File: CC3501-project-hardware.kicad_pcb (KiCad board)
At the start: 4 copper layers, 0 parts

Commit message: Recover autosave.
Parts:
- added C1: 22pF, Capacitor_SMD:C_0402_1005Metric, F.Cu at (469.1, 13.7)
- added C10: 100nF, Capacitor_SMD:C_0402_1005Metric, F.Cu at (449.4, 0.25)
- added C11: 100nF, Capacitor_SMD:C_0402_1005Metric, F.Cu at (449.4, 2.22)
- added C12: 100nF, Capacitor_SMD:C_0402_1005Metric, F.Cu at (449.4, 4.19)
- added C13: 100nF, Capacitor_SMD:C_0402_1005Metric, F.Cu at (449.4, 6.16)
- added C14: 100nF, Capacitor_SMD:C_0402_1005Metric, F.Cu at (449.4, 8.13)
- added C15: 100nF, Capacitor_SMD:C_0402_1005Metric, F.Cu at (452.2, 0.25)
- added C16: 100nF, Capacitor_SMD:C_0402_1005Metric, F.Cu at (452.2, 2.22)
- added C17: 100nF, Capacitor_SMD:C_0402_1005Metric, F.Cu at (452.2, 4.19)
- added C18: 100nF, Capacitor_SMD:C_0402_1005Metric, F.Cu at (404.7, 48.9)
- added C19: 10uF, Capacitor_SMD:C_0402_1005Metric, F.Cu at (384.0, 65.0)
- added C2: 10uF, Capacitor_SMD:C_0603_1608Metric, F.Cu at (473.7, 14.2)
- added C20: 100nF, Capacitor_SMD:C_0402_1005Metric, F.Cu at (384.0, 66.9)
- added C21: 10uF, Capacitor_SMD:C_0402_1005Metric, F.Cu at (384.0, 68.9)
- added C22: 100nF, Capacitor_SMD:C_0402_1005Metric, F.Cu at (384.0, 70.9)
- added C23: 22p NP0, Capacitor_SMD:C_0402_1005Metric, F.Cu at (392.0, 83.0)
- added C24: 22p NP0, Capacitor_SMD:C_0402_1005Metric, F.Cu at (392.0, 85.0)
- added C25: 62p NP0 2%, Capacitor_SMD:C_0805_2012Metric, F.Cu at (400.1, 83.6)
- added C26: 62p NP0 2%, Capacitor_SMD:C_0805_2012Metric, F.Cu at (400.1, 86.6)
- added C27: 56p, Capacitor_SMD:C_0603_1608Metric, F.Cu at (384.6, 83.3)
- added C28: 56p, Capacitor_SMD:C_0603_1608Metric, F.Cu at (384.6, 85.8)
- added C29: 270p NP0 2%, Capacitor_SMD:C_0603_1608Metric, F.Cu at (384.6, 88.3)
- added C3: 100nF, Capacitor_SMD:C_0402_1005Metric, F.Cu at (470.9, 48.3)
- added C30: 270p NP0 2%, Capacitor_SMD:C_0603_1608Metric, F.Cu at (384.6, 90.8)
- added C31: 270p NP0 2%, Capacitor_SMD:C_0603_1608Metric, F.Cu at (384.6, 93.4)
- added C32: 270p NP0 2%, Capacitor_SMD:C_0603_1608Metric, F.Cu at (384.6, 95.9)
- added C33: 100n X7R 10%, Capacitor_SMD:C_0603_1608Metric, F.Cu at (388.6, 83.3)
- added C34: 1n NP0 10%, Capacitor_SMD:C_0603_1608Metric, F.Cu at (388.6, 85.8)
- added C35: 100nF, Capacitor_SMD:C_0402_1005Metric, F.Cu at (392.0, 87.0)
- added C36: 100nF, Capacitor_SMD:C_0402_1005Metric, F.Cu at (392.0, 89.0)
- added C37: 100nF, Capacitor_SMD:C_0402_1005Metric, F.Cu at (392.0, 90.9)
- added C38: 100nF, Capacitor_SMD:C_0402_1005Metric, F.Cu at (392.0, 92.9)
- added C39: 100nF, Capacitor_SMD:C_0402_1005Metric, F.Cu at (384.0, 72.9)
- added C4: 33pF, Capacitor_SMD:C_0402_1005Metric, F.Cu at (487.1, 17.3)
- added C40: 100nF, Capacitor_SMD:C_0402_1005Metric, F.Cu at (384.0, 74.8)
- added C41: 100nF, Capacitor_SMD:C_0402_1005Metric, F.Cu at (384.0, 76.8)
- added C5: 33pF, Capacitor_SMD:C_0402_1005Metric, F.Cu at (491.5, 17.5)
- added C6: 10uF, Capacitor_SMD:C_0402_1005Metric, F.Cu at (451.1, 17.3)
- added C7: 1uF, Capacitor_SMD:C_0402_1005Metric, F.Cu at (470.9, 24.4)
- added C8: 1uF, Capacitor_SMD:C_0402_1005Metric, F.Cu at (473.9, 24.9)
- added C9: 100nF, Capacitor_SMD:C_0402_1005Metric, F.Cu at (446.5, 8.13)
- added D1: PRTR5V0U2X, Package_TO_SOT_SMD:SOT-143, F.Cu at (389.6, 37.8)
- added DS1: ILI9341, SamacSys_Parts:ILI9341, F.Cu at (342.8, 20.6)
- added J1: USB_C_Receptacle_USB2.0_16P, Connector_USB:USB_C_Receptacle_G-Switch_GT-USB-7010ASV, F.Cu at (453.0, 31.0)
- added J2: Conn_01x03_Socket, Connector_PinSocket_2.54mm:PinSocket_1x03_P2.54mm_Vertical, F.Cu at (406.6, 84.4)
- added J3: Conn_01x03_Socket, Connector_PinSocket_2.54mm:PinSocket_1x03_P2.54mm_Vertical, F.Cu at (411.2, 84.4)
- added J4: Conn_01x03_Socket, Connector_PinHeader_2.54mm:PinHeader_1x03_P2.54mm_Vertical, F.Cu at (394.5, 28.4)
- added J5: Conn_01x04_Socket, Connector_PinHeader_2.54mm:PinHeader_1x04_P2.54mm_Vertical, F.Cu at (377.9, 58.0)
- added J6: Conn_01x08_Socket, Connector_PinHeader_2.54mm:PinHeader_1x08_P2.54mm_Vertical, F.Cu at (377.9, 18.3)
- added J7: Conn_01x04, Connector_PinHeader_2.54mm:PinHeader_1x04_P2.54mm_Vertical, F.Cu at (387.7, 66.3)
- added J8: Conn_01x06_Socket, Connector_PinHeader_2.54mm:PinHeader_1x06_P2.54mm_Vertical, F.Cu at (377.9, 40.7)
- added JP1: SolderJumper_3_Bridged12, Jumper:SolderJumper-3_P1.3mm_Bridged12_RoundedPad1.0x1.5mm_NumberLabels, F.Cu at (413.6, 93.5)
- added JP4: SolderJumper_2_Bridged, Jumper:SolderJumper-2_P1.3mm_Bridged2Bar_RoundedPad1.0x1.5mm, F.Cu at (400.0, 77.4)
- added L1: 1uH, SamacSys_Parts:IND-SMD_L4.5-W4.0, F.Cu at (462.5, 19.6)
- added L2: 1uH, Inductor_SMD:L_0603_1608Metric, F.Cu at (388.6, 88.3)
- added L3: 1uH, Inductor_SMD:L_0603_1608Metric, F.Cu at (388.6, 90.8)
- added L4: 3.3uH, Inductor_SMD:L_0805_2012Metric, F.Cu at (387.7, 77.6)
- added P2: Header 1.27mm 2x5 PTH, Connector_PinHeader_1.27mm:PinHeader_2x05_P1.27mm_Vertical, F.Cu at (399.9, 43.7)
- added P3: Header 3, Connector_PinHeader_2.54mm:PinHeader_1x03_P2.54mm_Vertical, F.Cu at (393.4, 54.6)
- added Q1: SS8550, Package_TO_SOT_SMD:SOT-23, F.Cu at (392.5, 77.8)
- added Q3: AO3401A, Package_TO_SOT_SMD:SOT-23, F.Cu at (378.1, 76.0)
- added Q4: AO3401A, Package_TO_SOT_SMD:SOT-23, F.Cu at (383.8, 35.3)
- added R1: 5K1, Resistor_SMD:R_0201_0603Metric, F.Cu at (463.0, 34.6)
- added R10: 4.7k, Resistor_SMD:R_0603_1608Metric, F.Cu at (427.5, 74.4)
- added R11: 100, Resistor_SMD:R_0402_1005Metric, F.Cu at (431.8, 74.7)
- added R12: 100k, Resistor_SMD:R_0201_0603Metric, F.Cu at (477.1, 69.3)
- added R13: 27R, Resistor_SMD:R_0201_0603Metric, F.Cu at (376.9, 79.1)
- added R14: 100, Resistor_SMD:R_0402_1005Metric, F.Cu at (396.4, 76.6)
- added R15: 100, Resistor_SMD:R_0402_1005Metric, F.Cu at (396.4, 78.6)
- added R16: 20k, Resistor_SMD:R_0805_2012Metric, F.Cu at (400.7, 65.5)
- added R17: 8.2k, Resistor_SMD:R_0805_2012Metric, F.Cu at (400.7, 68.4)
- added R18: 10k, Resistor_SMD:R_0805_2012Metric, F.Cu at (397.9, 56.7)
- added R19: 10k, Resistor_SMD:R_0805_2012Metric, F.Cu at (400.7, 71.4)
- added R2: 5K1, Resistor_SMD:R_0201_0603Metric, F.Cu at (463.0, 36.3)
- added R20: 10k, Resistor_SMD:R_0805_2012Metric, F.Cu at (377.8, 69.3)
- added R21: 10k, Resistor_SMD:R_0805_2012Metric, F.Cu at (395.6, 83.5)
- added R22: 10k, Resistor_SMD:R_0805_2012Metric, F.Cu at (395.6, 86.5)
- added R23: 10k, Resistor_SMD:R_0805_2012Metric, F.Cu at (395.6, 89.4)
- added R24: 1k, Resistor_SMD:R_0402_1005Metric, F.Cu at (394.9, 99.2)
- added R25: 820R, Resistor_SMD:R_0603_1608Metric, F.Cu at (388.6, 93.4)
- added R26: 10k, Resistor_SMD:R_0805_2012Metric, F.Cu at (377.8, 72.3)
- added R27: 10k, Resistor_SMD:R_0805_2012Metric, F.Cu at (436.2, 74.9)
- added R3: 27R, Resistor_SMD:R_0201_0603Metric, F.Cu at (463.1, 30.0)
- added R4: 27R, Resistor_SMD:R_0201_0603Metric, F.Cu at (463.1, 32.8)
- added R5: 10k, Resistor_SMD:R_0805_2012Metric, F.Cu at (464.9, 42.9)
- added R6: 1k, Resistor_SMD:R_0402_1005Metric, F.Cu at (465.3, 46.7)
- added R7: 1k, Resistor_SMD:R_0402_1005Metric, F.Cu at (489.5, 29.0)
- added R8: 100k, Resistor_SMD:R_0603_1608Metric, F.Cu at (465.8, 21.8)
- added R9: 22.1k, Resistor_SMD:R_0603_1608Metric, F.Cu at (467.6, 23.6)
- added S1: TS-1187A-B-A-B, Button_Switch_SMD:SW_Push_1P1T_XKB_TS-1187A, F.Cu at (488.0, 44.1)
- added S2: TS-1187A-B-A-B, Button_Switch_SMD:SW_Push_1P1T_XKB_TS-1187A, F.Cu at (483.1, 69.8)
- added S3: TS-1187A-B-A-B, Button_Switch_SMD:SW_Push_1P1T_XKB_TS-1187A, F.Cu at (506.2, 44.6)
- added U1: RP2040, Package_DFN_QFN:QFN-56-1EP_7x7mm_P0.4mm_EP3.2x3.2mm, F.Cu at (474.0, 30.5)
- added U2: DS18B20, Package_TO_SOT_THT:TO-92_Inline, F.Cu at (428.0, 69.3)
- added U3: MFRC522, Package_DFN_QFN:VQFN-32-1EP_5x5mm_P0.5mm_EP3.1x3.1mm_ThermalVias, F.Cu at (428.8, 106.0)
- added U4: SY8089A1AAC, SamacSys_Parts:SOT95P285X130-5N, F.Cu at (462.5, 24.4)
- added U7: HX711, Package_SO:SOIC-16_3.9x9.9mm_P1.27mm, F.Cu at (451.4, 73.0)
- added U8: W25Q128JVSIQTR, lcsc:SOIC-8_L5.3-W5.3-P1.27-LS8.0-BL, F.Cu at (473.5, 43.7)
- added Y1: X322512MSB4SI, Crystal:Crystal_SMD_TXC_7M-4Pin_3.2x2.5mm, F.Cu at (487.3, 21.5)
- added Y2: Crystal_GND23, Crystal:Crystal_SMD_3225-4Pin_3.2x2.5mm, F.Cu at (428.4, 113.7)
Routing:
- net +5V: track 0.00 -> 13.8 mm
- net /USB_D_P: track 0.00 -> 9.01 mm
- net /USB_D_N: track 0.00 -> 8.98 mm
- net Net-(U4-FB): track 0.00 -> 7.80 mm
- net +3V3: track 0.00 -> 5.14 mm
- net GND: track 0.00 -> 3.81 mm, vias 0 -> 1

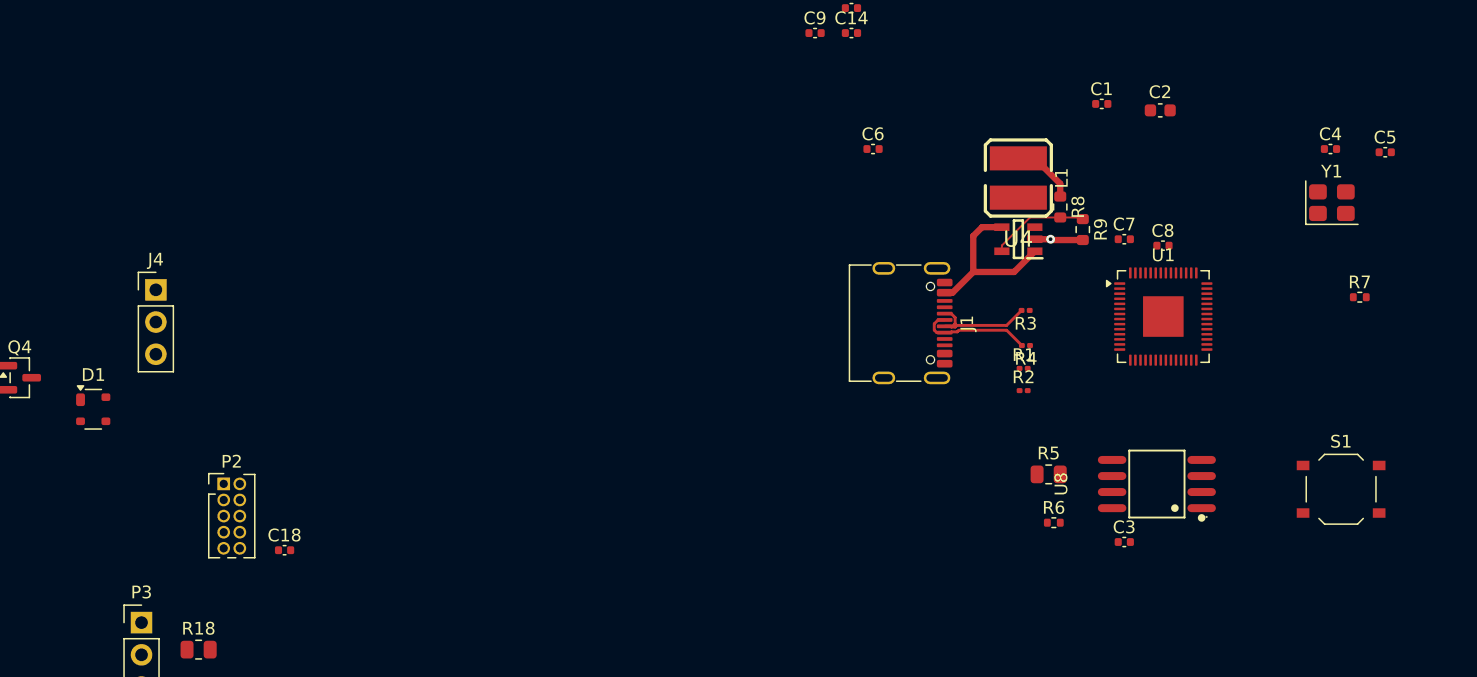
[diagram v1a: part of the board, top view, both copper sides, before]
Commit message: Layout the RP2040 basic components.
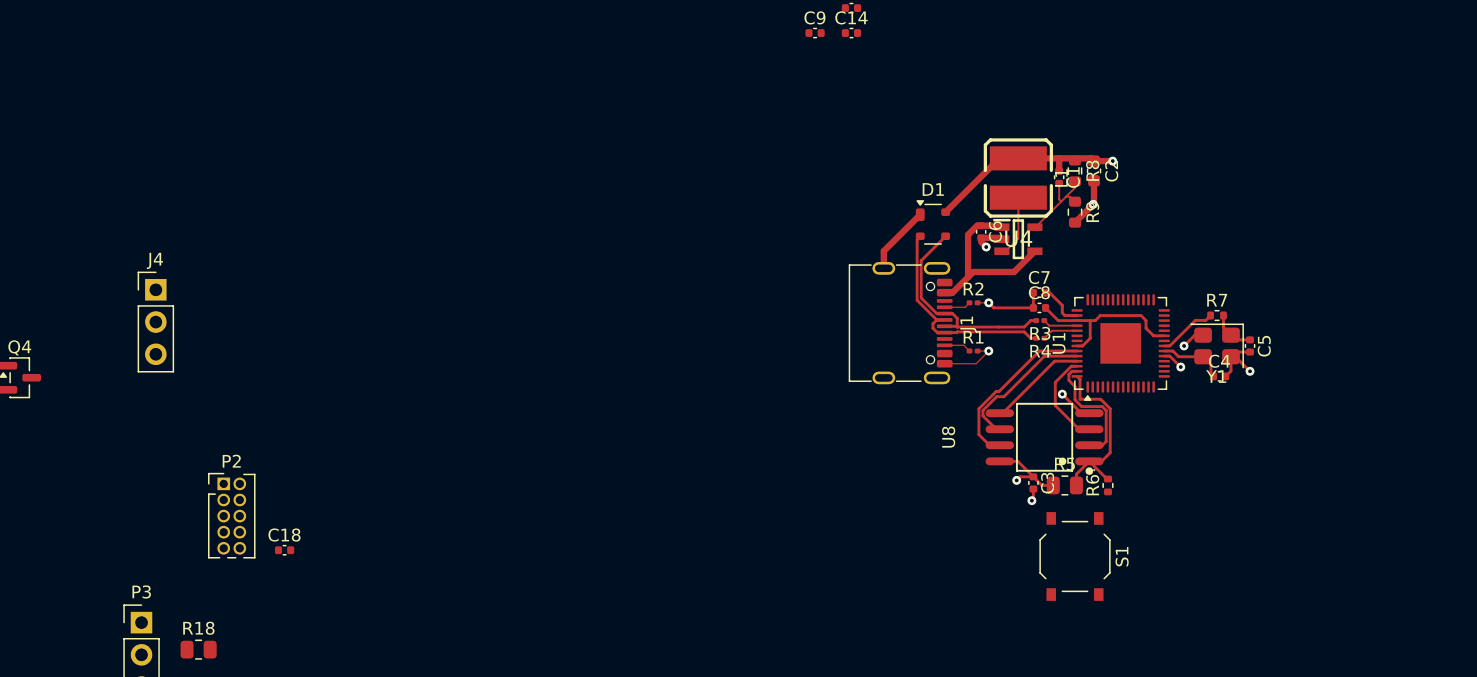
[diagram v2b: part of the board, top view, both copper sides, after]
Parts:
- moved D1 67.8 mm to (455.8, 23.2)
- moved S1 21.6 mm to (467.0, 49.4), turned to -90 degrees
- moved C4 19.9 mm to (478.4, 35.2)
- moved C5 18.6 mm to (480.8, 32.8), turned to -90 degrees
- moved Y1 14.5 mm to (478.2, 32.8), turned to 180 degrees
- moved R7 11.3 mm to (478.2, 30.4)
- moved C8 10.9 mm to (464.2, 29.8)
- moved C6 10.7 mm to (459.6, 23.8), turned to -90 degrees
- moved U8 9.59 mm to (464.6, 40.0)
- moved C3 8.55 mm to (463.7, 43.6), turned to -90 degrees
- moved R2 7.97 mm to (459.0, 29.4)
- moved C7 7.91 mm to (464.2, 28.6)
- moved C2 7.08 mm to (468.5, 19.0), turned to -90 degrees
- moved C1 6.69 mm to (465.8, 19.5), turned to -90 degrees
- moved R6 5.18 mm to (469.6, 43.8), turned to 90 degrees
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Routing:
- net GND: track 3.81 -> 35.2 mm, vias 1 -> 9
- net +3V3: track 5.14 -> 26.1 mm, vias 0 -> 2
- net /QSPI_CS: track 0.00 -> 14.4 mm
- net /QSPI_SD3: track 0.00 -> 13.9 mm
- net +1V1: track 0.00 -> 13.6 mm
- net /QSPI_SCLK: track 0.00 -> 11.6 mm
- net /QSPI_SD1: track 0.00 -> 9.65 mm
- net /USB_D_N: track 8.98 -> 17.3 mm
- net /USB_D_P: track 9.01 -> 17.3 mm
- net /QSPI_SD0: track 0.00 -> 7.79 mm
- net /QSPI_SD2: track 0.00 -> 7.53 mm
- net /XIN: track 0.00 -> 5.14 mm
- net Net-(U4-LX): track 0.00 -> 4.94 mm
- net /XOUT: track 0.00 -> 4.65 mm
- net Net-(Y1-CRYSTAL_1): track 0.00 -> 3.45 mm
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
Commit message: Assemble board.
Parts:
- removed DS1: ILI9341, SamacSys_Parts:ILI9341
- removed S1, S2, S3: TS-1187A-B-A-B, Button_Switch_SMD:SW_Push_1P1T_XKB_TS-1187A
- added G1: LOGO_PiicoDev, CoreElectronics_Artwork:piicodev_logo_14.2x3.4mm, F.Cu at (410.4, 153.5)
- added G7: Label_PCB_Art, PiicoDev RFID MFRC522:Art_2, F.Cu at (417.4, 153.5)
- added JP2: SolderJumper_3_Bridged12, Jumper:SolderJumper-3_P1.3mm_Bridged12_RoundedPad1.0x1.5mm_NumberLabels, F.Cu at (170.6, 45.6)
- added JP3: SolderJumper_3_Bridged12, Jumper:SolderJumper-3_P1.3mm_Bridged12_RoundedPad1.0x1.5mm_NumberLabels, F.Cu at (170.6, 48.3)
- added NT10: Net-Tie_2, PiicoDev RFID MFRC522:NetTie-2_SMD_Pad0.80mm, B.Cu at (150.6, 53.0)
- added NT11: Net-Tie_2, PiicoDev RFID MFRC522:NetTie-2_SMD_Pad0.80mm, B.Cu at (130.1, 56.0)
- added NT4: Net-Tie_2, PiicoDev RFID MFRC522:NetTie-2_SMD_Pad0.80mm, B.Cu at (151.6, 53.0)
- added NT8: Net-Tie_2_Top, PiicoDev RFID MFRC522:NetTie-2_SMD_Pad0.80mm, B.Cu at (127.9, 54.8)
- added NT9: Net-Tie_2_Top, PiicoDev RFID MFRC522:NetTie-2_SMD_Pad0.80mm, B.Cu at (129.0, 55.4)
- added SW1: SW_Push, Button_Switch_SMD:SW_Push_1P1T_XKB_TS-1187A, B.Cu at (203.4, 56.3)
- added SW2: SW_Push, Button_Switch_SMD:SW_Push_1P1T_XKB_TS-1187A, B.Cu at (203.4, 46.8)
- added SW3: SW_Push, Button_Switch_SMD:SW_Push_1P1T_XKB_TS-1187A, B.Cu at (201.0, 27.3)
- L2, L3: footprint Inductor_SMD:L_0603_1608Metric -> Inductor_SMD:L_0805_2012Metric
- moved C2 311.0 mm to (161.4, 68.3)
- moved R8 308.0 mm to (163.0, 68.3), turned to 90 degrees
- moved C5 306.4 mm to (174.9, 49.0), turned to 0 degrees
- moved R7 306.3 mm to (172.6, 51.6), turned to 90 degrees
- moved C1 305.4 mm to (164.3, 68.2), turned to 90 degrees
- moved R9 304.9 mm to (165.6, 68.3)
- moved Y1 303.9 mm to (174.9, 51.6), turned to -90 degrees
- moved L1 302.1 mm to (163.7, 64.0), turned to 0 degrees
- moved C4 301.6 mm to (177.3, 51.4), turned to 90 degrees
- moved U4 297.3 mm to (168.2, 66.8), turned to 90 degrees
- moved C7 297.1 mm to (169.2, 63.8), turned to 90 degrees
- moved U1 297.1 mm to (174.7, 59.2), turned to 180 degrees
- moved C6 295.5 mm to (167.7, 69.8), turned to 0 degrees
- moved C8 295.1 mm to (171.2, 64.3)
- moved R3 293.5 mm to (172.9, 65.6), turned to -90 degrees
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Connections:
- C27 pad 1: /RFID/TURN1A -> /RFID/TURN6B
- C28 pad 1: /RFID/TURN6B -> /RFID/TURN1A
- C29 pad 1: /RFID/TURN1A -> /RFID/TURN6B
- C30 pad 2: /RFID/TURN6B -> /RFID/TURN1A
- C31 pad 1: /RFID/TURN1A -> /RFID/TURN6B
- C32 pad 2: /RFID/TURN6B -> /RFID/TURN1A
- J6 pad 1: /LCD_LED -> /TFT Display/LED
- R13 pad 1: /LCD_LED -> /TFT Display/LED
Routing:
- net /TFT_MISO: track 0.00 -> 136.5 mm, vias 0 -> 2
- net /TFT_MOSI: track 0.00 -> 118.3 mm, vias 0 -> 3
- net /TFT_CLK: track 0.00 -> 108.6 mm, vias 0 -> 1
- net +5V: track 14.8 -> 116.0 mm, vias 0 -> 3
- net GND: track 35.2 -> 131.8 mm, vias 9 -> 33
- net +3V3: track 26.1 -> 95.3 mm, vias 2 -> 19
- net /SD_CS: track 0.00 -> 55.3 mm, vias 0 -> 1
- net /SW1: track 0.00 -> 53.0 mm, vias 0 -> 3
- net /RFID/TURN6B: track 0.00 -> 52.8 mm, vias 0 -> 3
- net /Temp_Data: track 0.00 -> 52.3 mm, vias 0 -> 4
- net /RUN: track 0.00 -> 50.4 mm, vias 0 -> 3
- net /LCD_CS: track 0.00 -> 49.4 mm, vias 0 -> 1
- net /SWCLK: track 0.00 -> 47.4 mm, vias 0 -> 4
- net /RFID/TURN1A: track 0.00 -> 46.9 mm, vias 0 -> 1
- net /UART_TX: track 0.00 -> 46.5 mm, vias 0 -> 2
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- added copper zone on In2.Cu, net +3V3
- added copper zone on In1.Cu, net GND
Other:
- board text added: "ASW"
- board text added: "RFID Module"

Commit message: Add edgecuts.
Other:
- board outline added: 85 x 56 mm
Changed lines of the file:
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@@
 		(layer "Dwgs.User")
+	)
+	(gr_rect
+		(start 123.5 25)
+		(end 208.5 81)
+		(stroke
+			(width 0.05)
+			(type default)
+		)
+		(fill no)
+		(layer "Edge.Cuts")
 	)
 	(image

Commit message: Generate production files.
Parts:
- removed J2, J3: Conn_01x03_Socket, Connector_PinSocket_2.54mm:PinSocket_1x03_P2.54mm_Vertical
- removed JP1: SolderJumper_3_Bridged12, Jumper:SolderJumper-3_P1.3mm_Bridged12_RoundedPad1.0x1.5mm_NumberLabels
- removed U2: DS18B20, Package_TO_SOT_THT:TO-92_Inline
- L2, L3: footprint Inductor_SMD:L_0805_2012Metric -> Inductor_SMD:L_0603_1608Metric
- moved SW3 0.51 mm to (200.8, 27.8)
- moved SW1 0.45 mm to (203.4, 56.8)
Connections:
- J5 pad 1: /SD_CS -> /TFT_CLK
- J5 pad 2: /TFT_MOSI -> /TFT_MISO
- J5 pad 3: /TFT_MISO -> /TFT_MOSI
- J5 pad 4: /TFT_CLK -> /SD_CS
- J6 pad 7: +5V -> GND
- J6 pad 8: GND -> +5V
- Q3 pad 1: /LCD_LED -> Net-(Q3-G)
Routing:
- net Net-(JP1-C): track 4.51 -> 0.00 mm
- net Temp_GND: track 4.00 -> 0.00 mm
- net +3V3: track 95.3 -> 97.3 mm, vias 19 -> 20
- net +5V: track 116.0 -> 115.1 mm

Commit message: ALL the PCB edits.
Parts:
- removed G1: LOGO_PiicoDev, CoreElectronics_Artwork:piicodev_logo_14.2x3.4mm
- removed G7: Label_PCB_Art, PiicoDev RFID MFRC522:Art_2
- added C42: 100nF, Capacitor_SMD:C_0402_1005Metric, F.Cu at (176.3, 35.8)
- added C43: 30pF, Capacitor_SMD:C_0201_0603Metric, F.Cu at (158.0, 50.5)
- added C44: 30pF, Capacitor_SMD:C_0201_0603Metric, F.Cu at (157.9, 55.4)
- added C45: 10p, Capacitor_SMD:C_0402_1005Metric, F.Cu at (156.9, 58.2)
- added C46: 10p, Capacitor_SMD:C_0402_1005Metric, F.Cu at (156.8, 47.7)
- added C47: 220pF, Capacitor_SMD:C_0402_1005Metric, F.Cu at (155.6, 50.9)
- added C48: 47pF, Capacitor_SMD:C_0402_1005Metric, F.Cu at (155.6, 51.9)
- added C49: 220pF, Capacitor_SMD:C_0402_1005Metric, F.Cu at (155.6, 54.1)
- added C50: 47pF, Capacitor_SMD:C_0402_1005Metric, F.Cu at (155.6, 55.1)
- added J9: Conn_01x02_Socket, Connector_PinHeader_2.54mm:PinHeader_1x02_P2.54mm_Vertical, F.Cu at (173.0, 32.0)
- added JP5: SolderJumper_2_Bridged, Jumper:SolderJumper-2_P1.3mm_Bridged2Bar_RoundedPad1.0x1.5mm, F.Cu at (192.5, 27.8)
- added R28: 100, Resistor_SMD:R_0402_1005Metric, F.Cu at (159.8, 61.0)
- added R29: 100k, Resistor_SMD:R_0603_1608Metric, F.Cu at (176.1, 34.5)
- C23, C24: value 22p NP0 -> 22pF C0G ±5%
- C25, C26: value 62p NP0 2% -> 33pF; footprint Capacitor_SMD:C_0805_2012Metric -> Capacitor_SMD:C_0402_1005Metric
- C27, C28: value 56p -> 47p; footprint Capacitor_SMD:C_0603_1608Metric -> Capacitor_SMD:C_0402_1005Metric
- C29, C30: value 270p NP0 2% -> 220pF; footprint Capacitor_SMD:C_0603_1608Metric -> Capacitor_SMD:C_0402_1005Metric
- C31, C32: value 270p NP0 2% -> 47pF; footprint Capacitor_SMD:C_0603_1608Metric -> Capacitor_SMD:C_0402_1005Metric
- C34: value 1n NP0 10% -> 1nF X7R ±10%
- L2, L3: footprint Inductor_SMD:L_0603_1608Metric -> Inductor_SMD:L_0805_2012Metric
- L4: value 3.3uH -> L; footprint Inductor_SMD:L_0805_2012Metric -> Inductor_THT:L_Axial_L11.0mm_D4.5mm_P15.24mm_Horizontal_Fastron_MECC
- R12, R3, R4: footprint Resistor_SMD:R_0201_0603Metric -> Resistor_SMD:R_0603_1608Metric
- SW1, SW2, SW3: footprint Button_Switch_SMD:SW_Push_1P1T_XKB_TS-1187A -> Button_Switch_THT:SW_SPST_Omron_B3F-40xx
- U3: value MFRC522 -> MFRC52202HN(TOKMAS)
- moved SW1 22.0 mm to (203.0, 78.8)
- moved J8 21.4 mm to (131.6, 74.0)
- moved J6 16.5 mm to (148.0, 74.0)
- moved SW2 16.0 mm to (203.0, 62.8)
- moved L4 14.9 mm to (185.5, 33.5)
- moved SW3 12.0 mm to (203.0, 39.5), turned to 90 degrees
- moved P2 11.9 mm to (182.0, 38.2), turned to 180 degrees
- moved R12 10.4 mm to (198.0, 42.7), turned to -90 degrees
- moved C18 7.69 mm to (195.8, 41.5), turned to -90 degrees
- moved C28 2.82 mm to (156.9, 59.2)
- moved C27 2.78 mm to (156.8, 46.7)
- moved C30 2.07 mm to (156.4, 57.1)
- moved R20 2.04 mm to (159.3, 66.0), turned to -90 degrees
- moved C31 1.92 mm to (155.6, 49.9)
- moved C32 1.90 mm to (155.6, 56.1)
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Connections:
- C26 pad 1: Net-(C26-Pad1) -> GND
- C26 pad 2: GND -> Net-(C26-Pad2)
- C28 pad 2: Net-(C26-Pad1) -> Net-(C26-Pad2)
- L2 pad 2: Net-(C26-Pad1) -> Net-(C26-Pad2)
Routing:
- net /TFT_CLK: track 108.6 -> 144.0 mm
- net Net-(JP5-A): track 18.4 -> 50.9 mm, vias 0 -> 1
- net /Limit_Switch: track 6.19 -> 35.1 mm, vias 1 -> 4
- net /Touch_CS: track 20.7 -> 46.3 mm
- net GND: track 131.8 -> 155.0 mm
- net /Touch_IRQ: track 27.9 -> 50.2 mm, vias 1 -> 3
- net Net-(J7-Pin_1): track 39.3 -> 61.4 mm
- net /TFT_MISO: track 136.5 -> 115.5 mm, vias 2 -> 3
- net /TFT Display/LED: track 32.3 -> 14.5 mm
- net /LCD_CS: track 49.4 -> 31.8 mm, vias 1 -> 2
- net /LCD_Data/CMD: track 43.6 -> 28.9 mm
- net +5V: track 115.1 -> 101.0 mm, vias 3 -> 2
- net /RUN: track 50.4 -> 64.4 mm, vias 3 -> 2
- net /LCD_RESET: track 40.6 -> 28.6 mm
- net /SWDIO: track 29.9 -> 41.5 mm
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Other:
- board text added: "2026 CC3501 ~ SMART FRIDGE DAMIEN TURNER ALISTER MALTBY NILS EISEN"
- board text added: "ASW I2C ADDR 1 2"
- board text added: "FLASH SW"
- board text added: "LF BYPASS"
- board text added: "PU BYPASS"
- board text added: "RUN SW"
- board text added: "USER SW"
- board text added: "[0 0] = 0x2C [1 0] = 0x2D [0 1] = 0x2E [1 1] = 0x2F"
- board text removed: "ASW"
- board text removed: "RFID Module"
